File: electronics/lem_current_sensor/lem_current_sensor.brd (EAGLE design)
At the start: 48.3 x 36.8 mm, 7 parts, among them J6 METALTEX-2, U1 LEM_LTS25_NP

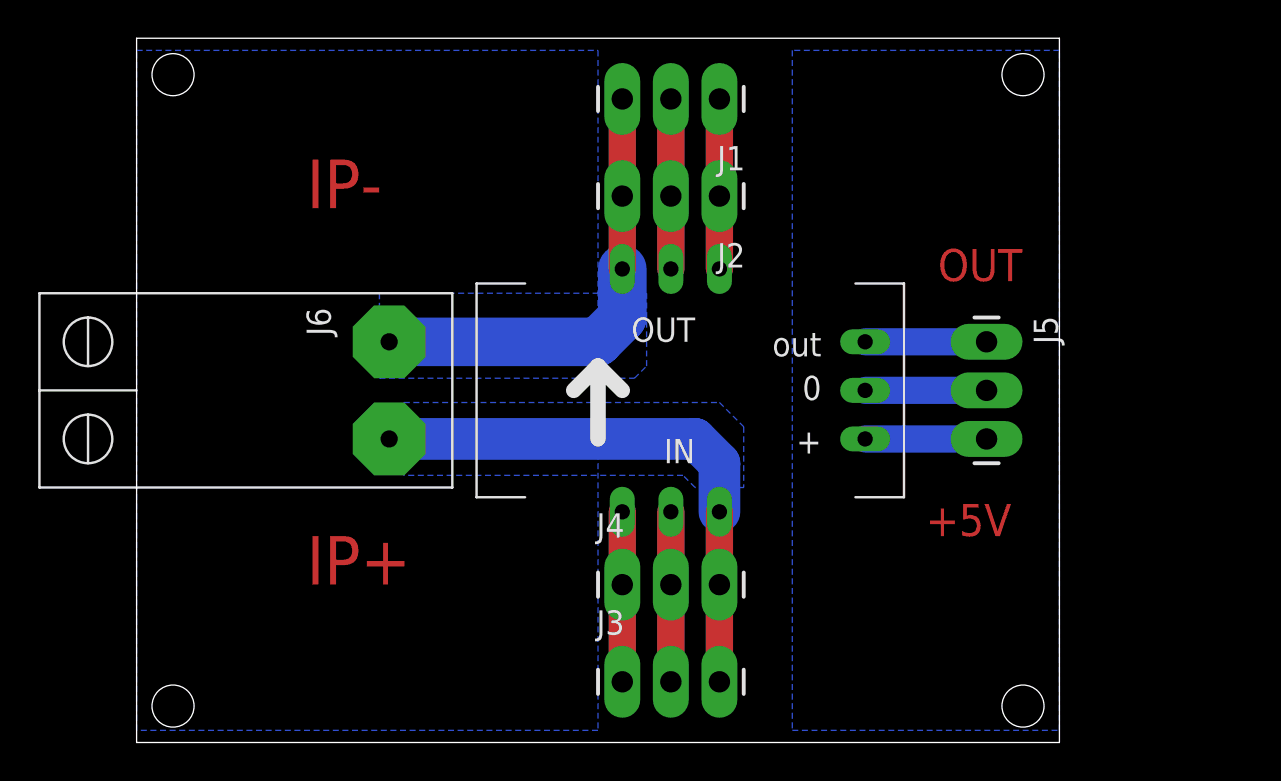
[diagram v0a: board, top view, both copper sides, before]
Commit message: Fix dimensions and MATLAB script for motor constants
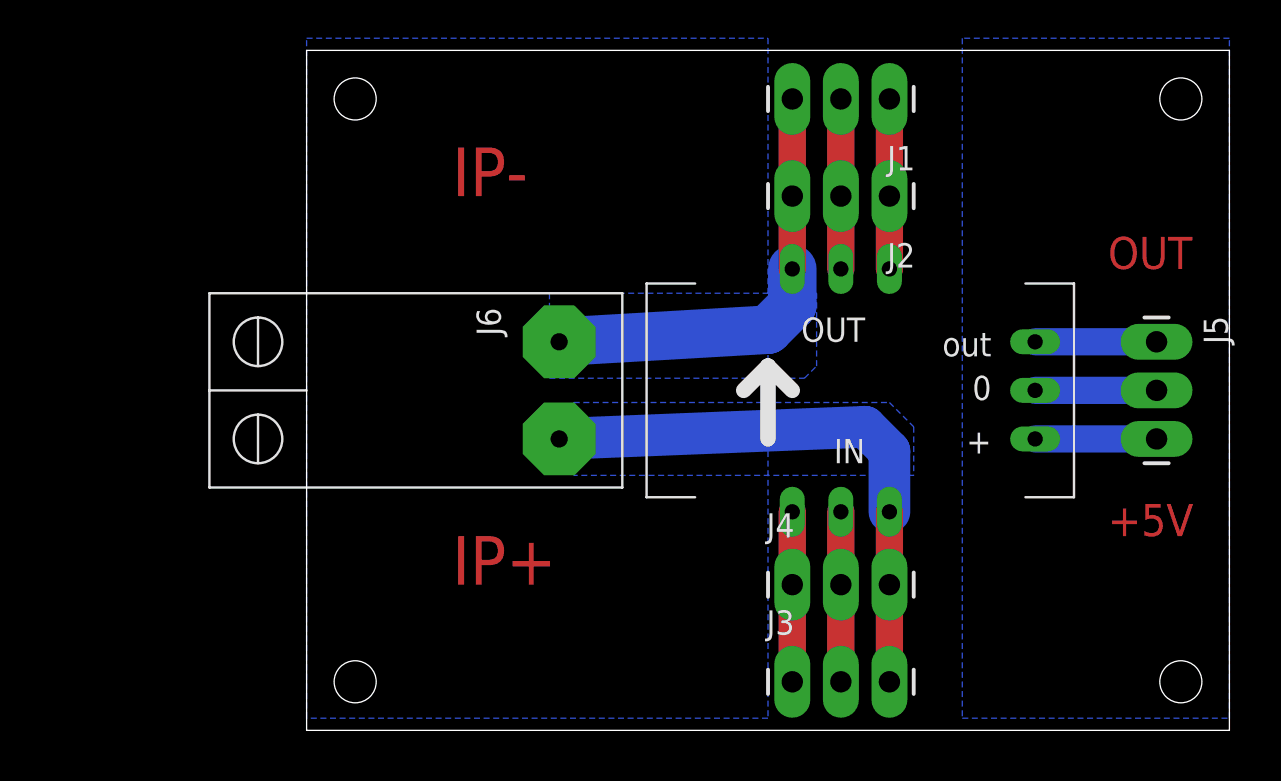
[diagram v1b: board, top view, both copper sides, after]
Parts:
- moved J1 8.89 mm to (30.5, 33.0)
- moved J2 8.89 mm to (30.5, 27.9)
- moved J5 8.89 mm to (44.5, 20.3)
- moved J6 8.89 mm to (11.4, 17.8)
- moved U1 8.89 mm to (38.1, 17.8)
- moved J3 8.89 mm to (25.4, 2.54)
- moved J4 8.89 mm to (25.4, 7.62)
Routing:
- net IP+: track 38.1 -> 38.8 mm
- net IP-: track 33.0 -> 32.4 mm
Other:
- board size 48.3 x 36.8 mm -> 48.3 x 35.6 mm
